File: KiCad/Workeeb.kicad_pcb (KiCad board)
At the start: 2 copper layers, 0 parts

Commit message: Finish setting values of switches, start PCB placement
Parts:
- added MX1: ESC, MX_Only:MXOnly-1U-NoLED, B.Cu at (23.8, 23.8)
- added MX10: 2, MX_Only:MXOnly-1U-NoLED, B.Cu at (570.4, 104.4)
- added MX101: -, MX_Only:MXOnly-1U-NoLED, B.Cu at (445.6, 82.3)
- added MX102: +, MX_Only:MXOnly-2U-NoLED, B.Cu at (615.6, 63.4)
- added MX103: Ent, MX_Only:MXOnly-2U-NoLED, B.Cu at (532.3, 42.5)
- added MX11: Q, MX_Only:MXOnly-1U-NoLED, B.Cu at (595.4, 124.6)
- added MX12: A, MX_Only:MXOnly-1U-NoLED, B.Cu at (460.9, 41.9)
- added MX13: Z, MX_Only:MXOnly-1U-NoLED, B.Cu at (486.0, 62.8)
- added MX14: F2, MX_Only:MXOnly-1U-NoLED, B.Cu at (600.1, 144.8)
- added MX15: 3, MX_Only:MXOnly-1U-NoLED, B.Cu at (550.2, 104.4)
- added MX16: W, MX_Only:MXOnly-1U-NoLED, B.Cu at (604.9, 165.0)
- added MX17: S, MX_Only:MXOnly-1U-NoLED, B.Cu at (506.2, 63.4)
- added MX18: X, MX_Only:MXOnly-1U-NoLED, B.Cu at (536.0, 83.6)
- added MX19: Alt, MX_Only:MXOnly-1.25U-NoLED, B.Cu at (593.0, 104.4)
- added MX2: ~~, MX_Only:MXOnly-1U-NoLED, B.Cu at (23.8, 52.4)
- added MX20: F3, MX_Only:MXOnly-1U-NoLED, B.Cu at (482.4, 42.5)
- added MX21: 4, MX_Only:MXOnly-1U-NoLED, B.Cu at (435.9, 21.7)
- added MX22: E, MX_Only:MXOnly-1U-NoLED, B.Cu at (575.2, 124.6)
- added MX23: D, MX_Only:MXOnly-1U-NoLED, B.Cu at (341.0, 62.1)
- added MX24: C, MX_Only:MXOnly-1U-NoLED, B.Cu at (408.8, 102.5)
- added MX25: F4, MX_Only:MXOnly-1U-NoLED, B.Cu at (385.0, 82.3)
- added MX26: 5, MX_Only:MXOnly-1U-NoLED, B.Cu at (546.6, 63.4)
- added MX27: R, MX_Only:MXOnly-1U-NoLED, B.Cu at (584.7, 165.0)
- added MX28: F, MX_Only:MXOnly-1U-NoLED, B.Cu at (530.0, 103.8)
- added MX29: V, MX_Only:MXOnly-1U-NoLED, B.Cu at (555.0, 124.6)
- added MX3: Tab, MX_Only:MXOnly-1.5U-NoLED, B.Cu at (620.3, 124.6)
- added MX30: 6, MX_Only:MXOnly-1U-NoLED, B.Cu at (580.0, 144.8)
- added MX31: T, MX_Only:MXOnly-1U-NoLED, B.Cu at (462.2, 62.1)
- added MX32: G, MX_Only:MXOnly-1U-NoLED, B.Cu at (559.8, 144.8)
- added MX33: B, MX_Only:MXOnly-1U-NoLED, B.Cu at (534.8, 124.6)
- added MX34: Space, MX_Only:MXOnly-6.25U-NoLED, B.Cu at (575.1, 21.7)
- added MX35: F5, MX_Only:MXOnly-1U-NoLED, B.Cu at (509.8, 103.8)
- added MX36: 7, MX_Only:MXOnly-1U-NoLED, B.Cu at (564.5, 165.0)
- added MX37: Y, MX_Only:MXOnly-1U-NoLED, B.Cu at (495.6, 83.6)
- added MX38: H, MX_Only:MXOnly-1U-NoLED, B.Cu at (625.1, 165.0)
- added MX39: N, MX_Only:MXOnly-1U-NoLED, B.Cu at (515.8, 83.6)
- added MX4: Caps Lock, MX_Only:MXOnly-1.75U-NoLED, B.Cu at (583.5, 84.2)
- added MX40: F6, MX_Only:MXOnly-1U-NoLED, B.Cu at (415.7, 21.7)
- added MX41: 8, MX_Only:MXOnly-1U-NoLED, B.Cu at (465.8, 82.3)
- added MX42: U, MX_Only:MXOnly-1U-NoLED, B.Cu at (489.6, 103.8)
- added MX43: J, MX_Only:MXOnly-1U-NoLED, B.Cu at (514.6, 124.0)
- added MX44: M, MX_Only:MXOnly-1U-NoLED, B.Cu at (442.0, 62.1)
- added MX45: F7, MX_Only:MXOnly-1U-NoLED, B.Cu at (544.3, 165.0)
- added MX46: 9, MX_Only:MXOnly-1U-NoLED, B.Cu at (420.5, 41.9)
- added MX47: I, MX_Only:MXOnly-1U-NoLED, B.Cu at (519.4, 144.8)
- added MX48: K, MX_Only:MXOnly-1U-NoLED, B.Cu at (395.5, 21.7)
- added MX49: ,, MX_Only:MXOnly-1U-NoLED, B.Cu at (469.4, 102.5)
- added MX5: Ctrl, MX_Only:MXOnly-1.25U-NoLED, B.Cu at (622.7, 144.8)
- added MX50: F8, MX_Only:MXOnly-1U-NoLED, B.Cu at (539.5, 144.8)
- added MX51: 0, MX_Only:MXOnly-1U-NoLED, B.Cu at (368.4, 102.5)
- added MX52: O, MX_Only:MXOnly-1U-NoLED, B.Cu at (524.1, 165.0)
- added MX53: L, MX_Only:MXOnly-1U-NoLED, B.Cu at (400.3, 41.9)
- added MX54: ., MX_Only:MXOnly-1U-NoLED, B.Cu at (499.1, 144.2)
- added MX55: R-Alt, MX_Only:MXOnly-1U-NoLED, B.Cu at (375.3, 21.7)
- added MX56: F9, MX_Only:MXOnly-1U-NoLED, B.Cu at (469.4, 122.7)
- added MX57: -, MX_Only:MXOnly-1U-NoLED, B.Cu at (449.2, 102.5)
- added MX58: P, MX_Only:MXOnly-1U-NoLED, B.Cu at (425.4, 82.3)
- added MX59: ;, MX_Only:MXOnly-1U-NoLED, B.Cu at (401.6, 62.1)
- added MX6: 1, MX_Only:MXOnly-1U-NoLED, B.Cu at (42.9, 52.4)
- added MX60: /, MX_Only:MXOnly-1U-NoLED, B.Cu at (503.9, 165.0)
- added MX61: Fn, MX_Only:MXOnly-1U-NoLED, B.Cu at (494.4, 124.0)
- added MX62: F10, MX_Only:MXOnly-1U-NoLED, B.Cu at (478.9, 144.2)
- added MX63: =, MX_Only:MXOnly-1U-NoLED, B.Cu at (463.5, 164.4)
- added MX64: [, MX_Only:MXOnly-1U-NoLED, B.Cu at (449.2, 122.7)
- added MX65: ', MX_Only:MXOnly-1U-NoLED, B.Cu at (429.0, 102.5)
- added MX66: R-Ctrl, MX_Only:MXOnly-1U-NoLED, B.Cu at (405.2, 82.3)
- added MX67: F11, MX_Only:MXOnly-1U-NoLED, B.Cu at (381.4, 62.1)
- added MX68: ], MX_Only:MXOnly-1U-NoLED, B.Cu at (483.7, 164.4)
- added MX69: Enter, MX_Only:MXOnly-2.25U-NoLED, B.Cu at (613.2, 42.5)
- added MX7: Shift, MX_Only:MXOnly-2.25U-NoLED, B.Cu at (493.0, 21.7)
- added MX70: Shift, MX_Only:MXOnly-1.75U-NoLED, B.Cu at (618.0, 84.2)
- added MX71: Left, MX_Only:MXOnly-1U-NoLED, B.Cu at (359.9, 41.9)
- added MX72: F12, MX_Only:MXOnly-1U-NoLED, B.Cu at (458.8, 142.9)
- added MX73: Backspace, MX_Only:MXOnly-2U-NoLED, B.Cu at (571.6, 42.5)
- added MX74: \, MX_Only:MXOnly-1.5U-NoLED, B.Cu at (620.3, 104.4)
- added MX75: Up, MX_Only:MXOnly-1U-NoLED, B.Cu at (334.9, 21.7)
- added MX76: Down, MX_Only:MXOnly-1U-NoLED, B.Cu at (355.1, 21.7)
- added MX77: Prnt Scrn, MX_Only:MXOnly-1U-NoLED, B.Cu at (361.2, 62.1)
- added MX78: Insert, MX_Only:MXOnly-1U-NoLED, B.Cu at (339.7, 41.9)
- added MX79: PgUp, MX_Only:MXOnly-1U-NoLED, B.Cu at (438.6, 142.9)
- added MX8: Win, MX_Only:MXOnly-1.25U-NoLED, B.Cu at (458.5, 21.7)
- added MX80: PgDn, MX_Only:MXOnly-1U-NoLED, B.Cu at (408.8, 122.7)
- added MX81: Delete, MX_Only:MXOnly-1U-NoLED, B.Cu at (388.6, 102.5)
- added MX82: Right, MX_Only:MXOnly-1U-NoLED, B.Cu at (364.8, 82.3)
- added MX83: Knob, Rotary_Encoder:RotaryEncoder_Alps_EC12E-Switch_Vertical_H20mm, B.Cu at (451.4, 178.6)
- added MX84: Num Lock, MX_Only:MXOnly-1U-NoLED, B.Cu at (443.3, 163.1)
- added MX85: 7, MX_Only:MXOnly-1U-NoLED, B.Cu at (429.0, 122.7)
- added MX86: 4, MX_Only:MXOnly-1U-NoLED, B.Cu at (418.4, 142.9)
- added MX87: 1, MX_Only:MXOnly-1U-NoLED, B.Cu at (388.6, 122.7)
- added MX89: /, MX_Only:MXOnly-1U-NoLED, B.Cu at (421.8, 62.1)
- added MX9: F1, MX_Only:MXOnly-1U-NoLED, B.Cu at (556.1, 84.2)
- added MX90: 8, MX_Only:MXOnly-1U-NoLED, B.Cu at (344.6, 82.3)
- added MX91: 5, MX_Only:MXOnly-1U-NoLED, B.Cu at (423.1, 163.1)
- added MX92: 2, MX_Only:MXOnly-1U-NoLED, B.Cu at (398.1, 142.9)
- added MX93: 0, MX_Only:MXOnly-2U-NoLED, B.Cu at (576.3, 63.4)
- added MX95: *, MX_Only:MXOnly-1U-NoLED, B.Cu at (368.4, 122.7)
- added MX96: 9, MX_Only:MXOnly-1U-NoLED, B.Cu at (348.2, 102.5)
- added MX97: 6, MX_Only:MXOnly-1U-NoLED, B.Cu at (402.9, 163.1)
- added MX98: 3, MX_Only:MXOnly-1U-NoLED, B.Cu at (377.9, 142.9)
- added MX99: ., MX_Only:MXOnly-1U-NoLED, B.Cu at (380.1, 41.9)

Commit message: Place some things and rename some stuff
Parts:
- added C1: 100nF, Capacitor_SMD:C_0805_2012Metric, F.Cu at (426.2, -19.1)
- added U1: STM32L412C8T6, STM32L412C8T6:STM32L412C8T6, F.Cu at (397.4, -10.6)
- MX1, MX10, MX11, MX12, MX13, MX14, MX15, MX16, MX17, MX18, MX19, MX2, MX20, MX21, MX22, MX23, MX24, MX25, MX26, MX27, MX28, MX29, MX3, MX30, MX31, MX32, MX33, MX34, MX35, MX36, MX37, MX38, MX39, MX4, MX40, MX41, MX42, MX43, MX44, MX45, MX46, MX47, MX48, MX49, MX5, MX50, MX51, MX52, MX53, MX54, MX55, MX56, MX57, MX58, MX59, MX6, MX60, MX61, MX62, MX63, MX64, MX65, MX66, MX67, MX68, MX69, MX7, MX71, MX72, MX73, MX74, MX75, MX76, MX77, MX78, MX79, MX8, MX80, MX81, MX82, MX83, MX84, MX9: moved to F.Cu
- MX101: value - -> num-; moved to F.Cu
- MX102: value + -> num+; moved to F.Cu
- MX103: value Ent -> numEnter; moved to F.Cu
- MX70: value Shift -> R-Shift; moved to F.Cu
- MX85: value 7 -> num7; moved to F.Cu
- MX86: value 4 -> num4; moved to F.Cu
- MX87: value 1 -> num1; moved to F.Cu
- MX89: value / -> num/; moved to F.Cu
- MX90: value 8 -> num8; moved to F.Cu
- MX91: value 5 -> num5; moved to F.Cu
- MX92: value 2 -> num2; moved to F.Cu
- MX93: value 0 -> num0; moved to F.Cu
- MX95: value * -> num*; moved to F.Cu
- MX96: value 9 -> num9; moved to F.Cu
- MX97: value 6 -> num6; moved to F.Cu
- MX98: value 3 -> num3; moved to F.Cu
- MX99: value . -> num.; moved to F.Cu
- moved MX5 596.8 mm to (26.2, 128.6), turned to 0 degrees
- moved MX3 594.2 mm to (28.6, 71.4), turned to 0 degrees
- moved MX102 571.6 mm to (75.0, -122.3), turned to 0 degrees
- moved MX4 552.6 mm to (31.0, 90.5), turned to 0 degrees
- moved MX11 545.6 mm to (52.4, 71.4), turned to 0 degrees
- moved MX16 541.6 mm to (71.4, 71.4), turned to 0 degrees
- moved MX14 533.1 mm to (81.0, 23.8), turned to 0 degrees
- moved MX19 519.8 mm to (73.8, 128.6), turned to 0 degrees
- moved MX10 511.2 mm to (61.9, 52.4), turned to 0 degrees
- moved MX93 498.0 mm to (114.2, -122.3), turned to 0 degrees
- moved MX9 497.9 mm to (61.9, 23.8), turned to 0 degrees
- moved MX22 487.6 mm to (90.5, 71.4), turned to 0 degrees
- moved MX27 484.3 mm to (109.5, 71.4), turned to 0 degrees
- moved MX38 478.6 mm to (152.4, 90.5), turned to 0 degrees
- moved MX15 472.1 mm to (81.0, 52.4), turned to 0 degrees
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
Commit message: Upgrade to KiCad6
Finish placing switches in PCB
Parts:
- removed C1: 100nF, Capacitor_SMD:C_0805_2012Metric
- removed U1: STM32L412C8T6, STM32L412C8T6:STM32L412C8T6
- MX102, MX103: footprint MX_Only:MXOnly-2U-NoLED -> MX_Only:MXOnly-2U-VerticalStabilizers-NoLED
- moved MX102 402.6 mm to (416.7, 90.5)
- moved MX103 375.1 mm to (416.7, 128.6)
- moved MX93 364.4 mm to (369.1, 138.1)
- moved MX99 295.1 mm to (397.7, 138.1)
- moved MX101 238.4 mm to (416.7, 61.9)
- moved MX89 215.6 mm to (378.6, 61.9)
- moved MX86 193.2 mm to (359.6, 100.0)
- moved MX87 191.0 mm to (359.6, 119.1)
- moved MX90 187.3 mm to (378.6, 81.0)
- moved MX92 183.4 mm to (378.6, 119.1)
- moved MX98 182.9 mm to (397.7, 119.1)
- moved MX85 174.2 mm to (359.6, 81.0)
- moved MX96 173.3 mm to (397.7, 81.0)
- moved MX91 164.3 mm to (378.6, 100.0)
- moved MX95 146.0 mm to (397.7, 61.9)
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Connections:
- MX83 pad A: Net-(MX83-PadA) -> unconnected-(MX83-PadA)
- MX83 pad B: Net-(MX83-PadB) -> unconnected-(MX83-PadB)
- MX83 pad C: Net-(MX83-PadC) -> unconnected-(MX83-PadC)
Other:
- net class Default removed

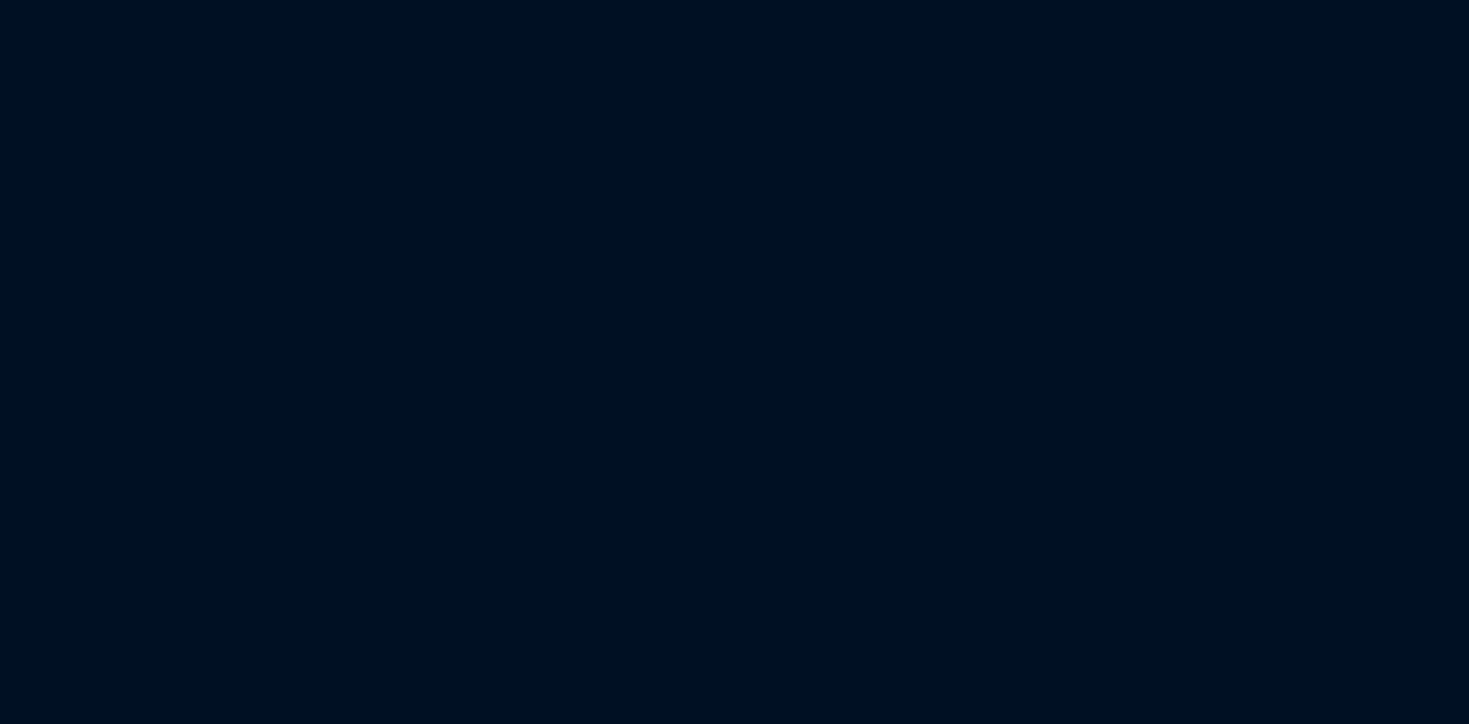
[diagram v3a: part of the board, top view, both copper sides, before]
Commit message: Match up the diodes and Elite-C footprint
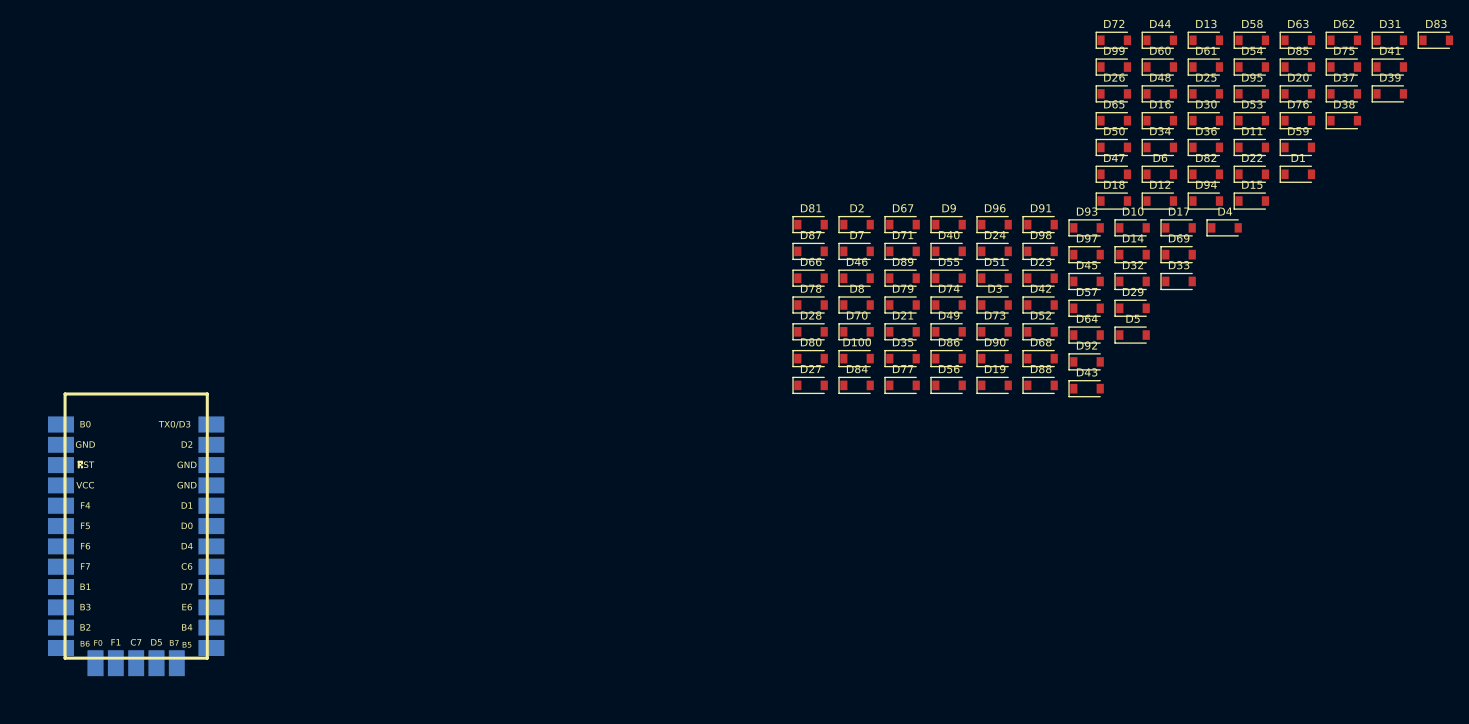
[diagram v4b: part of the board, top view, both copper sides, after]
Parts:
- added D1: D, Diode_SMD:D_SOD-123, F.Cu at (607.2, -11.9)
- added D10: D, Diode_SMD:D_SOD-123, F.Cu at (586.6, -5.21)
- added D100: D, Diode_SMD:D_SOD-123, F.Cu at (552.1, 11.1)
- added D11: D, Diode_SMD:D_SOD-123, F.Cu at (601.5, -15.3)
- added D12: D, Diode_SMD:D_SOD-123, F.Cu at (590.0, -8.56)
- added D13: D, Diode_SMD:D_SOD-123, F.Cu at (595.7, -28.7)
- added D14: D, Diode_SMD:D_SOD-123, F.Cu at (586.6, -1.86)
- added D15: D, Diode_SMD:D_SOD-123, F.Cu at (601.5, -8.56)
- added D16: D, Diode_SMD:D_SOD-123, F.Cu at (590.0, -18.6)
- added D17: D, Diode_SMD:D_SOD-123, F.Cu at (592.3, -5.21)
- added D18: D, Diode_SMD:D_SOD-123, F.Cu at (584.2, -8.56)
- added D19: D, Diode_SMD:D_SOD-123, F.Cu at (569.3, 14.5)
- added D2: D, Diode_SMD:D_SOD-123, F.Cu at (552.1, -5.62)
- added D20: D, Diode_SMD:D_SOD-123, F.Cu at (607.2, -22.0)
- added D21: D, Diode_SMD:D_SOD-123, F.Cu at (557.8, 7.78)
- added D22: D, Diode_SMD:D_SOD-123, F.Cu at (601.5, -11.9)
- added D23: D, Diode_SMD:D_SOD-123, F.Cu at (575.1, 1.08)
- added D24: D, Diode_SMD:D_SOD-123, F.Cu at (569.3, -2.27)
- added D25: D, Diode_SMD:D_SOD-123, F.Cu at (595.7, -22.0)
- added D26: D, Diode_SMD:D_SOD-123, F.Cu at (584.2, -22.0)
- added D27: D, Diode_SMD:D_SOD-123, F.Cu at (546.3, 14.5)
- added D28: D, Diode_SMD:D_SOD-123, F.Cu at (546.3, 7.78)
- added D29: D, Diode_SMD:D_SOD-123, F.Cu at (586.6, 4.84)
- added D3: D, Diode_SMD:D_SOD-123, F.Cu at (569.3, 4.43)
- added D30: D, Diode_SMD:D_SOD-123, F.Cu at (595.7, -18.6)
- added D31: D, Diode_SMD:D_SOD-123, F.Cu at (618.7, -28.7)
- added D32: D, Diode_SMD:D_SOD-123, F.Cu at (586.6, 1.49)
- added D33: D, Diode_SMD:D_SOD-123, F.Cu at (592.3, 1.49)
- added D34: D, Diode_SMD:D_SOD-123, F.Cu at (590.0, -15.3)
- added D35: D, Diode_SMD:D_SOD-123, F.Cu at (557.8, 11.1)
- added D36: D, Diode_SMD:D_SOD-123, F.Cu at (595.7, -15.3)
- added D37: D, Diode_SMD:D_SOD-123, F.Cu at (613.0, -22.0)
- added D38: D, Diode_SMD:D_SOD-123, F.Cu at (613.0, -18.6)
- added D39: D, Diode_SMD:D_SOD-123, F.Cu at (618.7, -22.0)
- added D4: D, Diode_SMD:D_SOD-123, F.Cu at (598.1, -5.21)
- added D40: D, Diode_SMD:D_SOD-123, F.Cu at (563.6, -2.27)
- added D41: D, Diode_SMD:D_SOD-123, F.Cu at (618.7, -25.3)
- added D42: D, Diode_SMD:D_SOD-123, F.Cu at (575.1, 4.43)
- added D43: D, Diode_SMD:D_SOD-123, F.Cu at (580.8, 14.9)
- added D44: D, Diode_SMD:D_SOD-123, F.Cu at (590.0, -28.7)
- added D45: D, Diode_SMD:D_SOD-123, F.Cu at (580.8, 1.49)
- added D46: D, Diode_SMD:D_SOD-123, F.Cu at (552.1, 1.08)
- added D47: D, Diode_SMD:D_SOD-123, F.Cu at (584.2, -11.9)
- added D48: D, Diode_SMD:D_SOD-123, F.Cu at (590.0, -22.0)
- added D49: D, Diode_SMD:D_SOD-123, F.Cu at (563.6, 7.78)
- added D5: D, Diode_SMD:D_SOD-123, F.Cu at (586.6, 8.19)
- added D50: D, Diode_SMD:D_SOD-123, F.Cu at (584.2, -15.3)
- added D51: D, Diode_SMD:D_SOD-123, F.Cu at (569.3, 1.08)
- added D52: D, Diode_SMD:D_SOD-123, F.Cu at (575.1, 7.78)
- added D53: D, Diode_SMD:D_SOD-123, F.Cu at (601.5, -18.6)
- added D54: D, Diode_SMD:D_SOD-123, F.Cu at (601.5, -25.3)
- added D55: D, Diode_SMD:D_SOD-123, F.Cu at (563.6, 1.08)
- added D56: D, Diode_SMD:D_SOD-123, F.Cu at (563.6, 14.5)
- added D57: D, Diode_SMD:D_SOD-123, F.Cu at (580.8, 4.84)
- added D58: D, Diode_SMD:D_SOD-123, F.Cu at (601.5, -28.7)
- added D59: D, Diode_SMD:D_SOD-123, F.Cu at (607.2, -15.3)
- added D6: D, Diode_SMD:D_SOD-123, F.Cu at (590.0, -11.9)
- added D60: D, Diode_SMD:D_SOD-123, F.Cu at (590.0, -25.3)
- added D61: D, Diode_SMD:D_SOD-123, F.Cu at (595.7, -25.3)
- added D62: D, Diode_SMD:D_SOD-123, F.Cu at (613.0, -28.7)
- added D63: D, Diode_SMD:D_SOD-123, F.Cu at (607.2, -28.7)
- added D64: D, Diode_SMD:D_SOD-123, F.Cu at (580.8, 8.19)
- added D65: D, Diode_SMD:D_SOD-123, F.Cu at (584.2, -18.6)
- added D66: D, Diode_SMD:D_SOD-123, F.Cu at (546.3, 1.08)
- added D67: D, Diode_SMD:D_SOD-123, F.Cu at (557.8, -5.62)
- added D68: D, Diode_SMD:D_SOD-123, F.Cu at (575.1, 11.1)
- added D69: D, Diode_SMD:D_SOD-123, F.Cu at (592.3, -1.86)
- added D7: D, Diode_SMD:D_SOD-123, F.Cu at (552.1, -2.27)
- added D70: D, Diode_SMD:D_SOD-123, F.Cu at (552.1, 7.78)
- added D71: D, Diode_SMD:D_SOD-123, F.Cu at (557.8, -2.27)
- added D72: D, Diode_SMD:D_SOD-123, F.Cu at (584.2, -28.7)
- added D73: D, Diode_SMD:D_SOD-123, F.Cu at (569.3, 7.78)
- added D74: D, Diode_SMD:D_SOD-123, F.Cu at (563.6, 4.43)
- added D75: D, Diode_SMD:D_SOD-123, F.Cu at (613.0, -25.3)
- added D76: D, Diode_SMD:D_SOD-123, F.Cu at (607.2, -18.6)
- added D77: D, Diode_SMD:D_SOD-123, F.Cu at (557.8, 14.5)
- added D78: D, Diode_SMD:D_SOD-123, F.Cu at (546.3, 4.43)
- added D79: D, Diode_SMD:D_SOD-123, F.Cu at (557.8, 4.43)
- added D8: D, Diode_SMD:D_SOD-123, F.Cu at (552.1, 4.43)
- added D80: D, Diode_SMD:D_SOD-123, F.Cu at (546.3, 11.1)
- added D81: D, Diode_SMD:D_SOD-123, F.Cu at (546.3, -5.62)
- added D82: D, Diode_SMD:D_SOD-123, F.Cu at (595.7, -11.9)
- added D83: D, Diode_SMD:D_SOD-123, F.Cu at (624.5, -28.7)
- added D84: D, Diode_SMD:D_SOD-123, F.Cu at (552.1, 14.5)
- added D85: D, Diode_SMD:D_SOD-123, F.Cu at (607.2, -25.3)
- added D86: D, Diode_SMD:D_SOD-123, F.Cu at (563.6, 11.1)
- added D87: D, Diode_SMD:D_SOD-123, F.Cu at (546.3, -2.27)
- added D88: D, Diode_SMD:D_SOD-123, F.Cu at (575.1, 14.5)
- added D89: D, Diode_SMD:D_SOD-123, F.Cu at (557.8, 1.08)
- added D9: D, Diode_SMD:D_SOD-123, F.Cu at (563.6, -5.62)
- added D90: D, Diode_SMD:D_SOD-123, F.Cu at (569.3, 11.1)
- added D91: D, Diode_SMD:D_SOD-123, F.Cu at (575.1, -5.62)
- added D92: D, Diode_SMD:D_SOD-123, F.Cu at (580.8, 11.5)
- added D93: D, Diode_SMD:D_SOD-123, F.Cu at (580.8, -5.21)
- added D94: D, Diode_SMD:D_SOD-123, F.Cu at (595.7, -8.56)
- added D95: D, Diode_SMD:D_SOD-123, F.Cu at (601.5, -22.0)
- added D96: D, Diode_SMD:D_SOD-123, F.Cu at (569.3, -5.62)
- added D97: D, Diode_SMD:D_SOD-123, F.Cu at (580.8, -1.86)
- added D98: D, Diode_SMD:D_SOD-123, F.Cu at (575.1, -2.27)
- added D99: D, Diode_SMD:D_SOD-123, F.Cu at (584.2, -25.3)
- added U1: Elite-C, Keebio-Parts:Elite-C-castellated-29pin, B.Cu at (462.0, 33.3)
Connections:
- MX1 pad 2: Net-(MX1-Pad2) -> Net-(D1-Pad2)
- MX10 pad 2: Net-(MX10-Pad2) -> Net-(D10-Pad2)
- MX101 pad 2: Net-(MX10-Pad2) -> Net-(D98-Pad2)
- MX102 pad 2: Net-(MX102-Pad2) -> Net-(D99-Pad2)
- MX103 pad 2: Net-(MX103-Pad2) -> Net-(D100-Pad2)
- MX11 pad 2: Net-(MX102-Pad2) -> Net-(D11-Pad2)
- MX12 pad 2: Net-(MX12-Pad2) -> Net-(D12-Pad2)
- MX13 pad 2: Net-(MX103-Pad2) -> Net-(D13-Pad2)
- MX14 pad 1: Net-(MX14-Pad1) -> Net-(MX10-Pad1)
- MX14 pad 2: Net-(MX1-Pad2) -> Net-(D14-Pad2)
- MX15 pad 1: Net-(MX14-Pad1) -> Net-(MX10-Pad1)
- MX15 pad 2: Net-(MX10-Pad2) -> Net-(D15-Pad2)
- MX16 pad 1: Net-(MX14-Pad1) -> Net-(MX10-Pad1)
- MX16 pad 2: Net-(MX102-Pad2) -> Net-(D16-Pad2)
- MX17 pad 1: Net-(MX14-Pad1) -> Net-(MX10-Pad1)
- MX17 pad 2: Net-(MX12-Pad2) -> Net-(D17-Pad2)
- MX18 pad 1: Net-(MX14-Pad1) -> Net-(MX10-Pad1)
- MX18 pad 2: Net-(MX103-Pad2) -> Net-(D18-Pad2)
- MX19 pad 1: Net-(MX14-Pad1) -> Net-(MX10-Pad1)
- MX19 pad 2: Net-(MX19-Pad2) -> Net-(D19-Pad2)
- MX2 pad 2: Net-(MX10-Pad2) -> Net-(D2-Pad2)
- MX20 pad 2: Net-(MX1-Pad2) -> Net-(D20-Pad2)
- MX21 pad 2: Net-(MX10-Pad2) -> Net-(D21-Pad2)
- MX22 pad 2: Net-(MX102-Pad2) -> Net-(D22-Pad2)
- MX23 pad 2: Net-(MX12-Pad2) -> Net-(D23-Pad2)
- MX24 pad 2: Net-(MX103-Pad2) -> Net-(D24-Pad2)
- MX25 pad 1: Net-(MX25-Pad1) -> Net-(MX20-Pad1)
- MX25 pad 2: Net-(MX1-Pad2) -> Net-(D25-Pad2)
- MX26 pad 1: Net-(MX25-Pad1) -> Net-(MX20-Pad1)
- MX26 pad 2: Net-(MX10-Pad2) -> Net-(D26-Pad2)
- MX27 pad 1: Net-(MX25-Pad1) -> Net-(MX20-Pad1)
- MX27 pad 2: Net-(MX102-Pad2) -> Net-(D27-Pad2)
- MX28 pad 1: Net-(MX25-Pad1) -> Net-(MX20-Pad1)
- MX28 pad 2: Net-(MX12-Pad2) -> Net-(D28-Pad2)
- MX29 pad 1: Net-(MX25-Pad1) -> Net-(MX20-Pad1)
- MX29 pad 2: Net-(MX103-Pad2) -> Net-(D29-Pad2)
- MX3 pad 2: Net-(MX102-Pad2) -> Net-(D3-Pad2)
- MX30 pad 2: Net-(MX10-Pad2) -> Net-(D30-Pad2)
- MX31 pad 2: Net-(MX102-Pad2) -> Net-(D31-Pad2)
- MX32 pad 2: Net-(MX12-Pad2) -> Net-(D32-Pad2)
- MX33 pad 2: Net-(MX103-Pad2) -> Net-(D33-Pad2)
- MX34 pad 2: Net-(MX19-Pad2) -> Net-(D34-Pad2)
- MX35 pad 1: Net-(MX35-Pad1) -> Net-(MX30-Pad1)
- MX35 pad 2: Net-(MX1-Pad2) -> Net-(D35-Pad2)
- MX36 pad 1: Net-(MX35-Pad1) -> Net-(MX30-Pad1)
- MX36 pad 2: Net-(MX10-Pad2) -> Net-(D36-Pad2)
- MX37 pad 1: Net-(MX35-Pad1) -> Net-(MX30-Pad1)
- MX37 pad 2: Net-(MX102-Pad2) -> Net-(D37-Pad2)
- MX38 pad 1: Net-(MX35-Pad1) -> Net-(MX30-Pad1)
- MX38 pad 2: Net-(MX12-Pad2) -> Net-(D38-Pad2)
- MX39 pad 1: Net-(MX35-Pad1) -> Net-(MX30-Pad1)
- MX39 pad 2: Net-(MX103-Pad2) -> Net-(D39-Pad2)
- MX4 pad 2: Net-(MX12-Pad2) -> Net-(D4-Pad2)
- MX40 pad 2: Net-(MX1-Pad2) -> Net-(D40-Pad2)
- MX41 pad 2: Net-(MX10-Pad2) -> Net-(D41-Pad2)
- MX42 pad 2: Net-(MX102-Pad2) -> Net-(D42-Pad2)
- MX43 pad 2: Net-(MX12-Pad2) -> Net-(D43-Pad2)
- MX44 pad 2: Net-(MX103-Pad2) -> Net-(D44-Pad2)
- MX45 pad 1: Net-(MX45-Pad1) -> Net-(MX40-Pad1)
- MX45 pad 2: Net-(MX1-Pad2) -> Net-(D45-Pad2)
- MX46 pad 1: Net-(MX45-Pad1) -> Net-(MX40-Pad1)
- MX46 pad 2: Net-(MX10-Pad2) -> Net-(D46-Pad2)
- MX47 pad 1: Net-(MX45-Pad1) -> Net-(MX40-Pad1)
- MX47 pad 2: Net-(MX102-Pad2) -> Net-(D47-Pad2)
- MX48 pad 1: Net-(MX45-Pad1) -> Net-(MX40-Pad1)
- MX48 pad 2: Net-(MX12-Pad2) -> Net-(D48-Pad2)
- MX49 pad 1: Net-(MX45-Pad1) -> Net-(MX40-Pad1)
- MX49 pad 2: Net-(MX103-Pad2) -> Net-(D49-Pad2)
- MX5 pad 2: Net-(MX19-Pad2) -> Net-(D5-Pad2)
- MX50 pad 2: Net-(MX1-Pad2) -> Net-(D50-Pad2)
- MX51 pad 2: Net-(MX10-Pad2) -> Net-(D51-Pad2)
- MX52 pad 2: Net-(MX102-Pad2) -> Net-(D52-Pad2)
- MX53 pad 2: Net-(MX12-Pad2) -> Net-(D53-Pad2)
- MX54 pad 2: Net-(MX103-Pad2) -> Net-(D54-Pad2)
- MX55 pad 2: Net-(MX19-Pad2) -> Net-(D55-Pad2)
- MX56 pad 1: Net-(MX56-Pad1) -> Net-(MX50-Pad1)
- MX56 pad 2: Net-(MX1-Pad2) -> Net-(D56-Pad2)
- MX57 pad 1: Net-(MX56-Pad1) -> Net-(MX50-Pad1)
- MX57 pad 2: Net-(MX10-Pad2) -> Net-(D57-Pad2)
- MX58 pad 1: Net-(MX56-Pad1) -> Net-(MX50-Pad1)
- MX58 pad 2: Net-(MX102-Pad2) -> Net-(D58-Pad2)
- MX59 pad 1: Net-(MX56-Pad1) -> Net-(MX50-Pad1)
- MX59 pad 2: Net-(MX12-Pad2) -> Net-(D59-Pad2)
- MX6 pad 1: Net-(MX6-Pad1) -> Net-(MX1-Pad1)
- MX6 pad 2: Net-(MX10-Pad2) -> Net-(D6-Pad2)
- MX60 pad 1: Net-(MX56-Pad1) -> Net-(MX50-Pad1)
- MX60 pad 2: Net-(MX103-Pad2) -> Net-(D60-Pad2)
- MX61 pad 1: Net-(MX56-Pad1) -> Net-(MX50-Pad1)
- MX61 pad 2: Net-(MX19-Pad2) -> Net-(D61-Pad2)
- MX62 pad 2: Net-(MX1-Pad2) -> Net-(D62-Pad2)
- MX63 pad 2: Net-(MX10-Pad2) -> Net-(D63-Pad2)
- MX64 pad 2: Net-(MX102-Pad2) -> Net-(D64-Pad2)
- MX65 pad 2: Net-(MX12-Pad2) -> Net-(D65-Pad2)
- MX66 pad 2: Net-(MX19-Pad2) -> Net-(D66-Pad2)
- MX67 pad 1: Net-(MX67-Pad1) -> Net-(MX62-Pad1)
- MX67 pad 2: Net-(MX1-Pad2) -> Net-(D67-Pad2)
- MX68 pad 1: Net-(MX67-Pad1) -> Net-(MX62-Pad1)
- MX68 pad 2: Net-(MX102-Pad2) -> Net-(D68-Pad2)
- MX69 pad 1: Net-(MX67-Pad1) -> Net-(MX62-Pad1)
- MX69 pad 2: Net-(MX12-Pad2) -> Net-(D69-Pad2)
- MX7 pad 1: Net-(MX6-Pad1) -> Net-(MX1-Pad1)
- MX7 pad 2: Net-(MX103-Pad2) -> Net-(D7-Pad2)
- MX70 pad 1: Net-(MX67-Pad1) -> Net-(MX62-Pad1)
- MX70 pad 2: Net-(MX103-Pad2) -> Net-(D70-Pad2)
- MX71 pad 1: Net-(MX67-Pad1) -> Net-(MX62-Pad1)
- MX71 pad 2: Net-(MX19-Pad2) -> Net-(D71-Pad2)
- MX72 pad 2: Net-(MX1-Pad2) -> Net-(D72-Pad2)
- MX73 pad 2: Net-(MX10-Pad2) -> Net-(D73-Pad2)
- MX74 pad 2: Net-(MX102-Pad2) -> Net-(D74-Pad2)
- MX75 pad 2: Net-(MX103-Pad2) -> Net-(D75-Pad2)
- MX76 pad 2: Net-(MX19-Pad2) -> Net-(D76-Pad2)
- MX77 pad 1: Net-(MX77-Pad1) -> Net-(MX72-Pad1)
- MX77 pad 2: Net-(MX1-Pad2) -> Net-(D77-Pad2)
- MX78 pad 1: Net-(MX77-Pad1) -> Net-(MX72-Pad1)
- MX78 pad 2: Net-(MX10-Pad2) -> Net-(D78-Pad2)
- MX79 pad 1: Net-(MX77-Pad1) -> Net-(MX72-Pad1)
- MX79 pad 2: Net-(MX102-Pad2) -> Net-(D79-Pad2)
- MX8 pad 1: Net-(MX6-Pad1) -> Net-(MX1-Pad1)
- MX8 pad 2: Net-(MX19-Pad2) -> Net-(D8-Pad2)
- MX80 pad 1: Net-(MX77-Pad1) -> Net-(MX72-Pad1)
- MX80 pad 2: Net-(MX12-Pad2) -> Net-(D80-Pad2)
- MX81 pad 1: Net-(MX77-Pad1) -> Net-(MX72-Pad1)
- MX81 pad 2: Net-(MX103-Pad2) -> Net-(D81-Pad2)
- MX82 pad 1: Net-(MX77-Pad1) -> Net-(MX72-Pad1)
- MX82 pad 2: Net-(MX19-Pad2) -> Net-(D82-Pad2)
- MX83 pad S2: Net-(MX1-Pad2) -> Net-(D83-Pad2)
- MX84 pad 2: Net-(MX10-Pad2) -> Net-(D84-Pad2)
- MX85 pad 2: Net-(MX102-Pad2) -> Net-(D85-Pad2)
- MX86 pad 2: Net-(MX12-Pad2) -> Net-(D86-Pad2)
- MX87 pad 2: Net-(MX103-Pad2) -> Net-(D87-Pad2)
- MX89 pad 1: Net-(MX89-Pad1) -> Net-(MX83-PadS1)
- MX89 pad 2: Net-(MX10-Pad2) -> Net-(D88-Pad2)
- MX9 pad 2: Net-(MX1-Pad2) -> Net-(D9-Pad2)
- MX90 pad 1: Net-(MX89-Pad1) -> Net-(MX83-PadS1)
- MX90 pad 2: Net-(MX102-Pad2) -> Net-(D89-Pad2)
- MX91 pad 1: Net-(MX89-Pad1) -> Net-(MX83-PadS1)
- MX91 pad 2: Net-(MX12-Pad2) -> Net-(D90-Pad2)
- MX92 pad 1: Net-(MX89-Pad1) -> Net-(MX83-PadS1)
- MX92 pad 2: Net-(MX103-Pad2) -> Net-(D91-Pad2)
- MX93 pad 1: Net-(MX89-Pad1) -> Net-(MX83-PadS1)
- MX93 pad 2: Net-(MX19-Pad2) -> Net-(D92-Pad2)
- MX95 pad 1: Net-(MX95-Pad1) -> Net-(MX101-Pad1)
- MX95 pad 2: Net-(MX10-Pad2) -> Net-(D93-Pad2)
- MX96 pad 1: Net-(MX95-Pad1) -> Net-(MX101-Pad1)
- MX96 pad 2: Net-(MX102-Pad2) -> Net-(D94-Pad2)
- MX97 pad 1: Net-(MX95-Pad1) -> Net-(MX101-Pad1)
- MX97 pad 2: Net-(MX12-Pad2) -> Net-(D95-Pad2)
- MX98 pad 1: Net-(MX95-Pad1) -> Net-(MX101-Pad1)
- MX98 pad 2: Net-(MX103-Pad2) -> Net-(D96-Pad2)
- MX99 pad 1: Net-(MX95-Pad1) -> Net-(MX101-Pad1)
- MX99 pad 2: Net-(MX19-Pad2) -> Net-(D97-Pad2)
